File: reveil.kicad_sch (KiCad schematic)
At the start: 22 parts, among them J1 Barrel_Jack_Switch, J2 AudioJack3_SwitchTR, M1 Motor_DC, Q1 2N3904, Q2 IRLB8721PBF

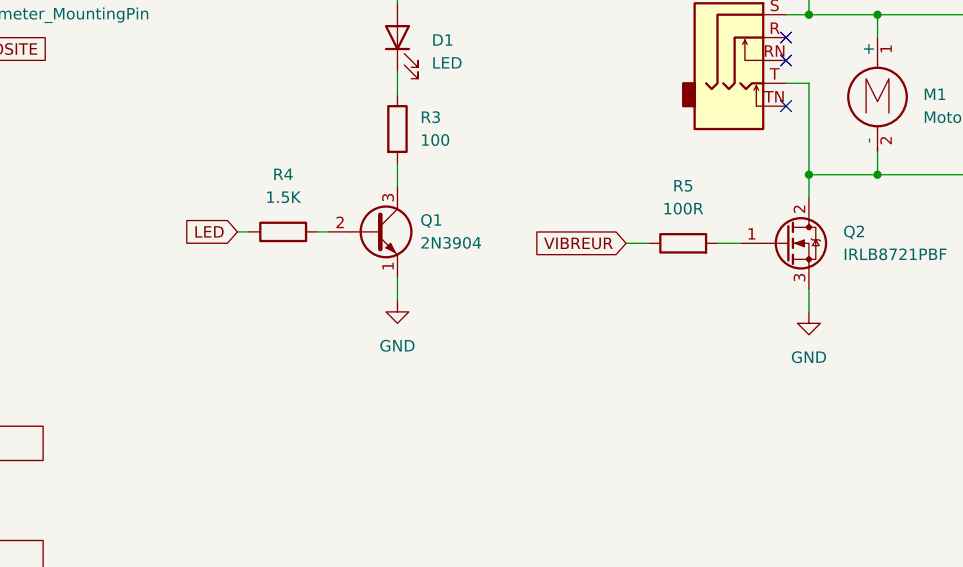
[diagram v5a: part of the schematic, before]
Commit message: Schéma/PCB : ajoute les pull-down de grille Q2 et de base Q1
GPIO18 est en haute impédance pendant le boot/reset du Pico. Sans rien
pour fixer son potentiel, la grille de Q2 pouvait flotter à un niveau
intermédiaire (vibration intempestive du moteur, ou Q2 à moitié
passant qui chauffe), et la base de Q1 pouvait aussi flotter et le
faire conduire légèrement, ce qui aurait pu repousser du courant vers
la grille de Q2 à travers R5.

Ajoute :
- R6 (100 kΩ) entre la grille et la source de Q2 (donc vers GND,
  Source étant déjà relié à GND)
- R7 (47 kΩ) entre la base et l'émetteur de Q1, pour garder Q1
  déterministement bloqué pendant que sa base flotte

Empreintes placées et pistes routées sur le PCB.

Connectivité vérifiée via le netlist KiCad (R6 sur Net-(Q2-G) avec Q2-G
et R5 ; R7 sur Net-(Q1-B) avec Q1-B et R4 ; R6 et R7 tous deux sur le
net GND avec Q2-S et Q1-E) et ERC/DRC revérifiés via le conteneur
Docker KiBot : 0 erreur/avertissement ERC ; DRC revenu à la référence
(6 avertissements silk_edge_clearance préexistants sur J2), aucun
écart schéma/PCB.

Co-Authored-By: Claude Sonnet 5 <noreply@anthropic.com>
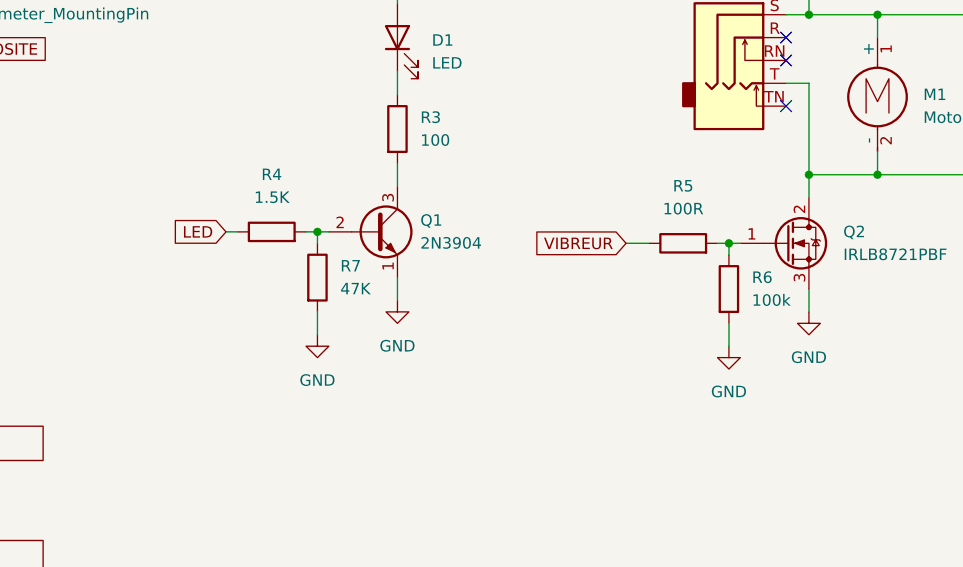
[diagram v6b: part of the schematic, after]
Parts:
- added R6: 100k, Resistor_THT:R_Axial_DIN0207_L6.3mm_D2.5mm_P7.62mm_Horizontal, symbol Device:R
- added R7: 47K, Resistor_THT:R_Axial_DIN0207_L6.3mm_D2.5mm_P7.62mm_Horizontal, symbol Device:R
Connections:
- net GND: now also R6.2, R7.2
- net at Q2.1 (G), R5.2: now also R6.1
- net at Q1.2 (B), R4.2: now also R7.1
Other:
- moved on the sheet: R4

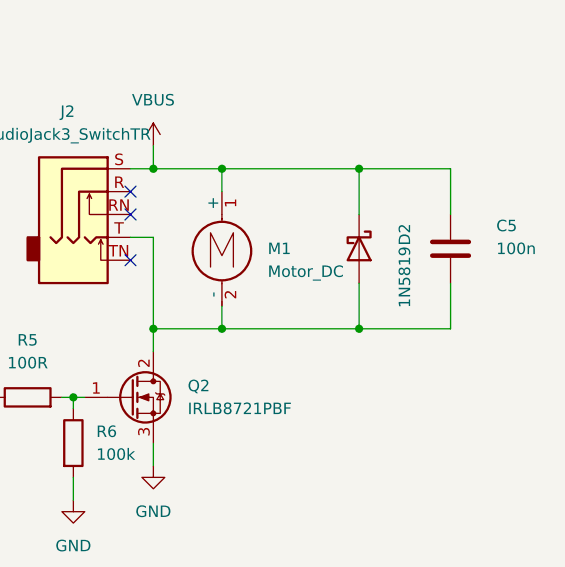
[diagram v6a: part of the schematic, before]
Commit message: Schéma/PCB : unifie D2 sur 1N5822 pour simplifier la BOM
D2 (roue libre moteur) était en 1N5819 (1A). Passe en 1N5822 (3A) pour
n'avoir qu'une seule référence de Schottky dans tout le projet : la
diode prévue pour protéger VSYS contre le retour du jack J1 (section
Alimentation du README) sera aussi une 1N5822, choisie avec de la
marge faute de datasheet pour le courant moteur réel.

Même boîtier DO-41 THT, même tension inverse (40V), même datasheet
Vishay (doc 88525, couvre déjà toute la famille 1N5817-1N5822) : seule
la Value change, schéma et PCB.

ERC/DRC revérifiés via le conteneur Docker KiBot : 0 erreur/avertissement
ERC, DRC inchangé (6 avertissements silk_edge_clearance préexistants
sur J2).

Co-Authored-By: Claude Sonnet 5 <noreply@anthropic.com>
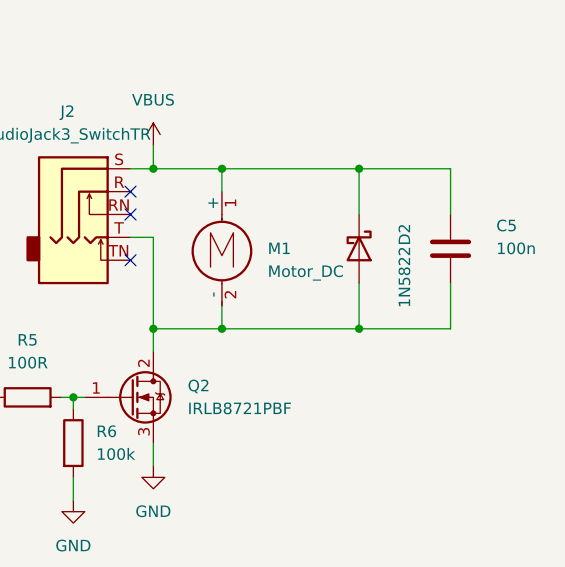
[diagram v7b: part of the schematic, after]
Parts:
- D2: value 1N5819 -> 1N5822
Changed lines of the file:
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@@
 			)
 		)
-		(property "Value" "1N5819"
+		(property "Value" "1N5822"
 			(at 267.97 128 0)
 			(effects
